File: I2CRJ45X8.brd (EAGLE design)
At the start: 80 x 50 mm, 54 parts, among them IC1 MCP23017SO, IC2 MCP23017SO, J1 M02X3-SHROUDED, J3 M02X3-PIN, J4 M02X3-PIN, J5 RJ45-X8, J6 M02X3-SHROUDED

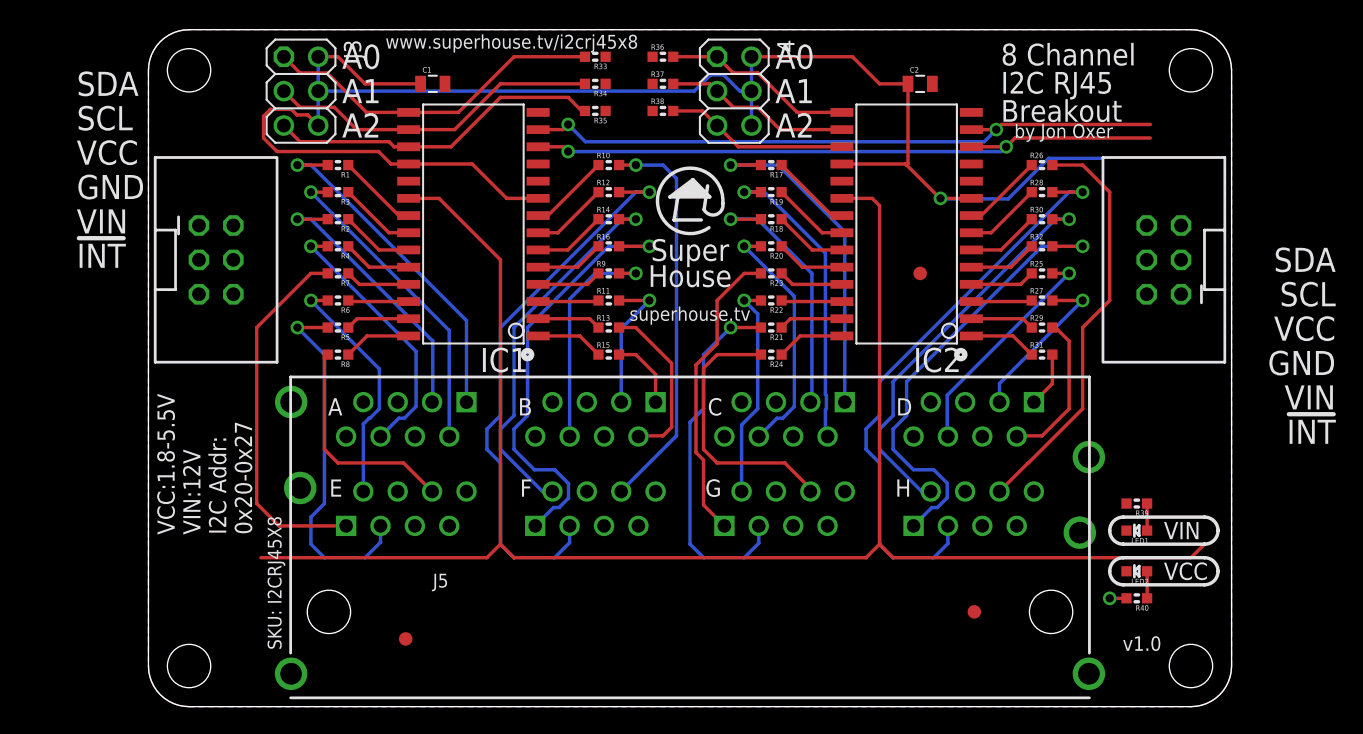
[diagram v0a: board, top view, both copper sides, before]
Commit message: Routing for I2C Breakout headers
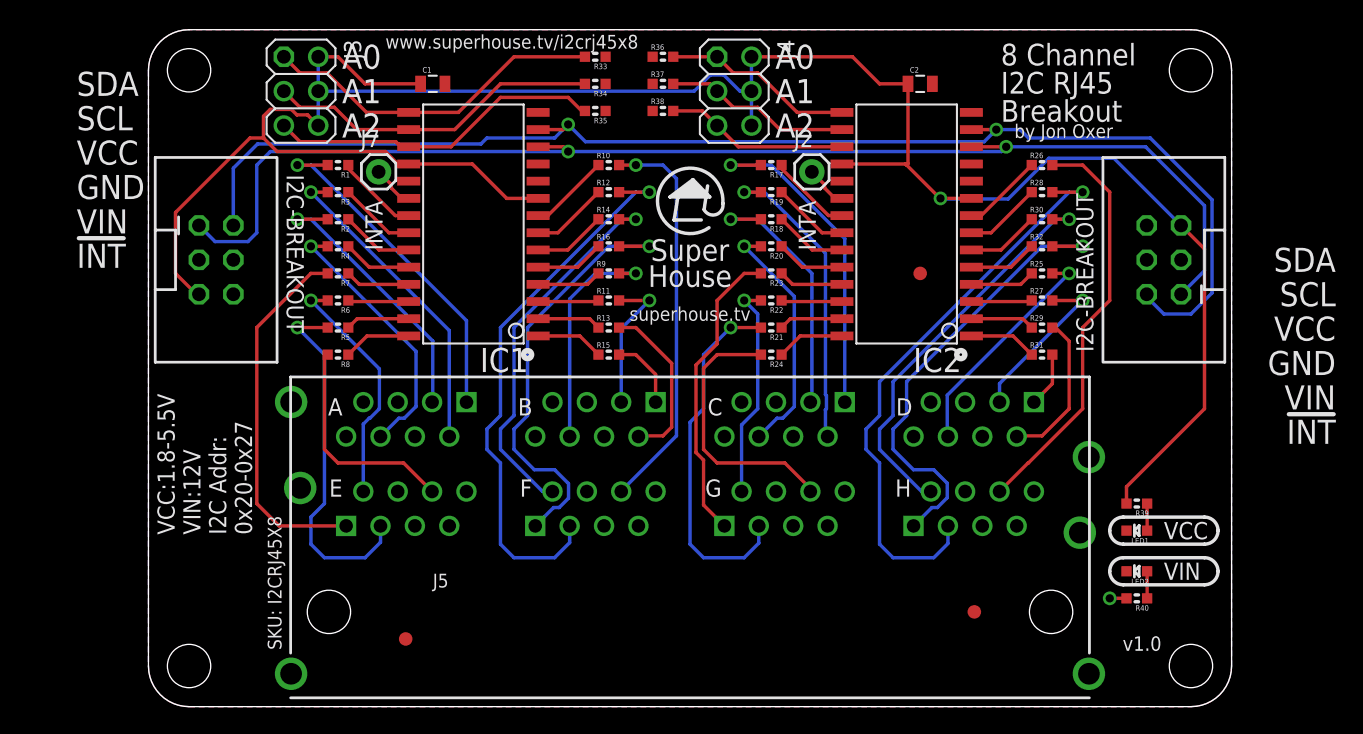
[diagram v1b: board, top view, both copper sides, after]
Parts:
- added J2: INT2A, SuperHouse-Connectors:1X01
- added J7: INT1A, SuperHouse-Connectors:1X01
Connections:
- removed net !INT: IC1.20, IC2.20
- new net N$10: IC1.20, J7.1
- new net N$9: IC2.20, J2.1
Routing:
- net !INT: track 129.4 -> 0.00 mm
- net SDA: track 48.3 -> 98.2 mm
- net VCC: track 122.6 -> 169.7 mm
- net SCL: track 48.3 -> 94.6 mm
- net N$9: track 0.00 -> 3.18 mm
- net N$10: track 0.00 -> 3.18 mm
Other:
- board text added: "I2C-BREAKOUT"
- board text added: "INTA"

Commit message: Experimenting with options for linking MCP reset to I2C Breakout reset
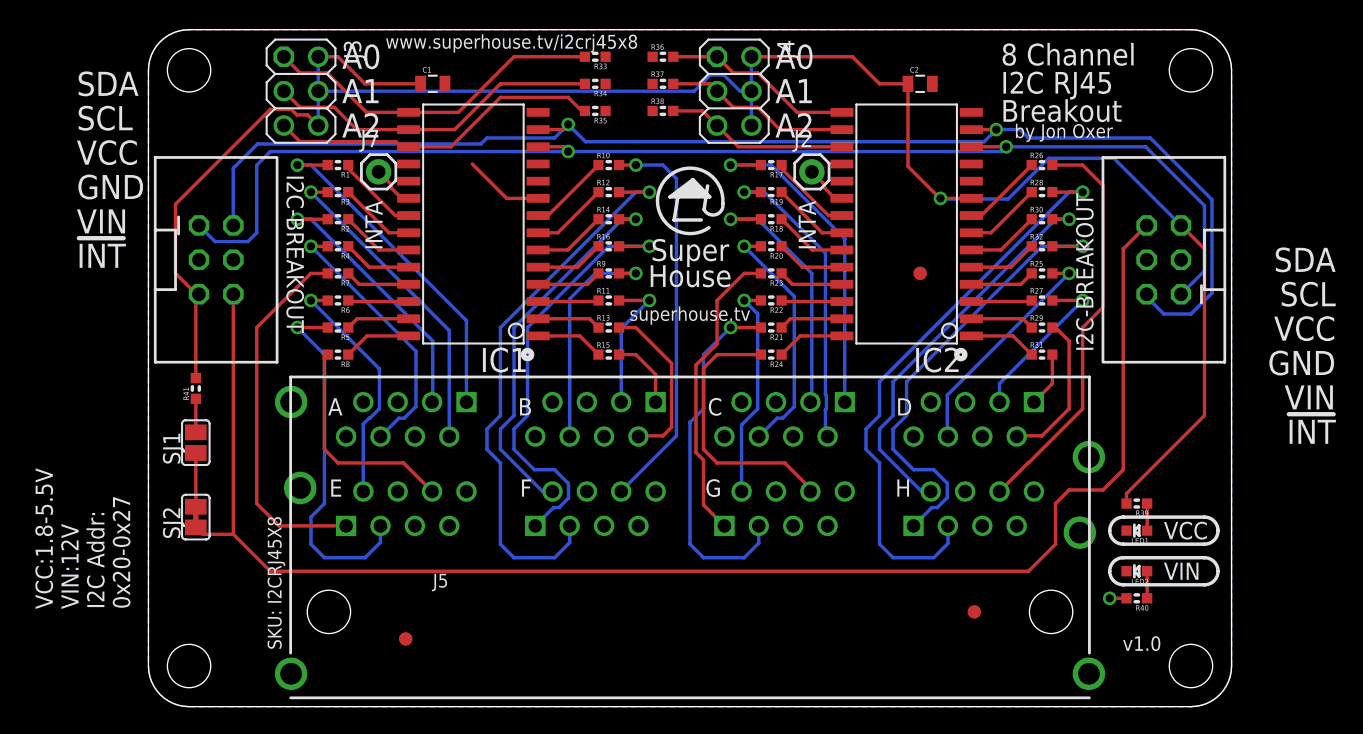
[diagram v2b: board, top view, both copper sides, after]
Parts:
- added R41: 10K, SuperHouse-DiscreteSemi:R0603
- added SJ1: (no value), SuperHouse-Jumpers:SJ
- added SJ2: SJC-NORMAL, SuperHouse-Jumpers:SJC
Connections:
- new net !RST: IC1.18, IC2.18, SJ1.1, SJ2.2
- new net N$14: R41.1, SJ1.2
- net !RESET: now also SJ2.1
- net VCC: now also R41.2; no longer IC1.18, IC2.18
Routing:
- net !RESET: track 0.00 -> 111.2 mm
- net VCC: track 169.7 -> 154.3 mm
- net !RST: track 0.00 -> 3.98 mm
- net N$14: track 0.00 -> 2.48 mm
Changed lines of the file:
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@@
 House</text>
 <text x="40" y="28.5" size="1.016" layer="21" font="vector" ratio="17" distance="20" align="bottom-center">superhouse.tv</text>
-<text x="4.16" y="12.7" size="1.27" layer="21" font="vector" ratio="18" rot="R90" align="center-left">VCC:1.8-5.5V
+<text x="-4.84" y="7.2" size="1.27" layer="21" font="vector" ratio="18" rot="R90" align="center-left">VCC:1.8-5.5V
 VIN:12V
 I2C Addr:
@@
 <attribute name="VALUE" x="15.73" y="36.325" size="1.27" layer="27"/>
 </element>
+<element name="SJ1" library="SuperHouse-Jumpers" library_urn="urn:adsk.eagle:library:12190622" package="SJ" package3d_urn="urn:adsk.eagle:package:7066338/1" value="" x="3.5" y="19.5" smashed="yes" rot="R90">
+<attribute name="NAME" x="2.357" y="17.849" size="1.27" layer="25" ratio="10" rot="R90"/>
+<attribute name="VALUE" x="3.5" y="19.9001" size="0.02" layer="27" rot="R90"/>
+</element>
+<element name="SJ2" library="SuperHouse-Jumpers" library_urn="urn:adsk.eagle:library:12190622" package="SJC" package3d_urn="urn:adsk.eagle:package:7066342/1" value="SJC-NORMAL" x="3.5" y="14" smashed="yes" rot="R90">
+<attribute name="NAME" x="2.357" y="12.349" size="1.27" layer="25" ratio="10" rot="R90"/>
+<attribute name="VALUE" x="3.5" y="14.4001" size="0.02" layer="27" rot="R90"/>
+</element>
+<element name="R41" library="SuperHouse-DiscreteSemi" library_urn="urn:adsk.eagle:library:11768461" package="R0603" package3d_urn="urn:adsk.eagle:package:11768543/2" value="10K" x="3.5" y="23.5" smashed="yes" rot="R90">
+<attribute name="NAME" x="2.992" y="22.611" size="0.4064" layer="25" font="vector" rot="R90"/>
+<attribute name="VALUE" x="4.4652" y="22.484" size="0.4064" layer="27" font="vector" rot="R90"/>
+</element>
 </elements>
 <signals>
@@
 <wire x1="65" y1="18" x2="69" y2="22" width="0.254" layer="1"/>
 <wire x1="69" y1="22" x2="69" y2="28" width="0.254" layer="1"/>
-<wire x1="69" y1="28" x2="71" y2="30" width="0.254" layer="1"/>
-<wire x1="71" y1="30" x2="71" y2="38" width="0.254" layer="1"/>
-<wire x1="71" y1="38" x2="69" y2="40" width="0.254" layer="1"/>
+<wire x1="69" y1="28" x2="70.5" y2="29.5" width="0.254" layer="1"/>
+<wire x1="70.5" y1="29.5" x2="70.5" y2="38.5" width="0.254" layer="1"/>
+<wire x1="70.5" y1="38.5" x2="69" y2="40" width="0.254" layer="1"/>
 <wire x1="69" y1="40" x2="66.762" y2="40" width="0.254" layer="1"/>
 </signal>
@@
 </signal>
 <signal name="VCC">
-<contactref element="IC1" pad="18"/>
 <contactref element="IC1" pad="9"/>
-<contactref element="IC2" pad="18"/>
 <contactref element="IC2" pad="9"/>
 <contactref element="J3" pad="6"/>
@@
 <contactref element="J3" pad="2"/>
 <wire x1="26.46" y1="37.54" x2="28.78" y2="37.54" width="0.254" layer="1"/>
-<wire x1="19.22" y1="40.08" x2="23.92" y2="40.08" width="0.254" layer="1"/>
 <wire x1="58.46" y1="37.54" x2="58.5" y2="37.54" width="0.254" layer="1"/>
 <wire x1="58.5" y1="37.54" x2="60.78" y2="37.54" width="0.254" layer="1"/>
-<wire x1="55.92" y1="40.08" x2="51.22" y2="40.08" width="0.254" layer="1"/>
 <contactref element="C1" pad="1"/>
-<wire x1="56" y1="40" x2="55.92" y2="40.08" width="0.254" layer="1"/>
 <wire x1="23.92" y1="40.08" x2="26.46" y2="37.54" width="0.254" layer="1"/>
-<wire x1="56" y1="40" x2="58.46" y2="37.54" width="0.254" layer="1"/>
 <contactref element="C2" pad="1"/>
-<wire x1="56.1" y1="46" x2="56.1" y2="40.1" width="0.254" layer="1"/>
-<wire x1="56.1" y1="40.1" x2="56" y2="40" width="0.254" layer="1"/>
 <contactref element="J4" pad="6"/>
 <contactref element="J4" pad="4"/>
@@
 <wire x1="54" y1="46" x2="52" y2="48" width="0.254" layer="1"/>
 <wire x1="52" y1="48" x2="44.54" y2="48" width="0.254" layer="1"/>
-<wire x1="19.22" y1="40.08" x2="18.42" y2="40.08" width="0.254" layer="1"/>
-<wire x1="18.42" y1="40.08" x2="17.5" y2="41" width="0.254" layer="1"/>
-<wire x1="9.5" y1="41" x2="8.5" y2="42" width="0.254" layer="1"/>
-<wire x1="8.5" y1="43.6138" x2="8.5" y2="42" width="0.254" layer="1"/>
-<wire x1="17.5" y1="41" x2="9.5" y2="41" width="0.254" layer="1"/>
 <wire x1="10.55593125" y1="44.1138" x2="9" y2="44.1138" width="0.254" layer="1"/>
-<wire x1="9" y1="44.1138" x2="8.5" y2="43.6138" width="0.254" layer="1"/>
 <wire x1="63.5" y1="37.5" x2="66.5" y2="40.5" width="0.254" layer="16"/>
 <wire x1="63.5" y1="37.5" x2="58.5" y2="37.5" width="0.254" layer="16"/>
@@
 <wire x1="71.31" y1="40.5" x2="76.27" y2="35.54" width="0.254" layer="16"/>
 <wire x1="66.5" y1="40.5" x2="71.31" y2="40.5" width="0.254" layer="16"/>
-<wire x1="72.238" y1="15" x2="72.238" y2="16.238" width="0.254" layer="1"/>
-<wire x1="72.238" y1="16.238" x2="78" y2="22" width="0.254" layer="1"/>
+<wire x1="72.238" y1="15" x2="72.238" y2="15.738" width="0.254" layer="1"/>
+<wire x1="72.238" y1="15.738" x2="78" y2="21.5" width="0.254" layer="1"/>
 <wire x1="78" y1="33.81" x2="76.27" y2="35.54" width="0.254" layer="1"/>
-<wire x1="78" y1="22" x2="78" y2="33.81" width="0.254" layer="1"/>
+<wire x1="78" y1="21.5" x2="78" y2="33.81" width="0.254" layer="1"/>
 <wire x1="3.73" y1="30.46" x2="3.54" y2="30.46" width="0.254" layer="1"/>
-<wire x1="3.54" y1="30.46" x2="2" y2="32" width="0.254" layer="1"/>
-<wire x1="2" y1="32" x2="2" y2="36.5" width="0.254" layer="1"/>
-<wire x1="2" y1="36.5" x2="7.5" y2="42" width="0.254" layer="1"/>
-<wire x1="7.5" y1="42" x2="8.5" y2="42" width="0.254" layer="1"/>
+<wire x1="2" y1="32" x2="3.54" y2="30.46" width="0.254" layer="1"/>
+<contactref element="R41" pad="2"/>
+<wire x1="9" y1="44.1138" x2="2" y2="37.1138" width="0.254" layer="1"/>
+<wire x1="2" y1="37.1138" x2="2" y2="32" width="0.254" layer="1"/>
+<wire x1="56.1" y1="39.9" x2="58.46" y2="37.54" width="0.254" layer="1"/>
+<wire x1="56.1" y1="46" x2="56.1" y2="39.9" width="0.254" layer="1"/>
+<wire x1="3.5" y1="24.262" x2="3.5" y2="30.23" width="0.254" layer="1"/>
+<wire x1="3.5" y1="30.23" x2="3.73" y2="30.46" width="0.254" layer="1"/>
+<wire x1="20.1" y1="46" x2="23.92" y2="40.08" width="0" layer="19" extent="1-1"/>
 </signal>
 <signal name="N$2">
@@
 <contactref element="J6" pad="6"/>
 <contactref element="J1" pad="6"/>
-<wire x1="6.27" y1="30.46" x2="73.73" y2="35.54" width="0" layer="19" extent="1-1"/>
+<contactref element="SJ2" pad="1"/>
+<wire x1="73.73" y1="35.54" x2="72" y2="33.81" width="0.254" layer="1"/>
+<wire x1="72" y1="17.5" x2="70.5" y2="16" width="0.254" layer="1"/>
+<wire x1="68" y1="16" x2="67" y2="15" width="0.254" layer="1"/>
+<wire x1="67" y1="12" x2="65" y2="10" width="0.254" layer="1"/>
+<wire x1="9" y1="10" x2="6.27" y2="12.73" width="0.254" layer="1"/>
+<wire x1="6.27" y1="12.73" x2="6.27" y2="30.46" width="0.254" layer="1"/>
+<wire x1="72" y1="33.81" x2="72" y2="17.5" width="0.254" layer="1"/>
+<wire x1="70.5" y1="16" x2="68" y2="16" width="0.254" layer="1"/>
+<wire x1="67" y1="15" x2="67" y2="12" width="0.254" layer="1"/>
+<wire x1="65" y1="10" x2="9" y2="10" width="0.254" layer="1"/>
+<wire x1="4.008" y1="12.73" x2="3.5" y2="13.238" width="0.254" layer="1"/>
+<wire x1="6.27" y1="12.73" x2="4.008" y2="12.73" width="0.254" layer="1"/>
 </signal>
 <signal name="N$9">
@@
 <wire x1="18.70434375" y1="37.54" x2="17.9382" y2="38.30614375" width="0.254" layer="1"/>
 </signal>
+<signal name="!RST">
+<contactref element="SJ1" pad="1"/>
+<contactref element="SJ2" pad="2"/>
+<contactref element="IC1" pad="18"/>
+<contactref element="IC2" pad="18"/>
+<wire x1="3.5" y1="18.738" x2="3.5" y2="14.762" width="0.254" layer="1"/>
+<wire x1="19.22" y1="40.08" x2="51.22" y2="40.08" width="0" layer="19" extent="1-1"/>
+<wire x1="3.5" y1="18.738" x2="19.22" y2="40.08" width="0" layer="19" extent="1-1"/>
+</signal>
+<signal name="N$14">
+<contactref element="R41" pad="1"/>
+<contactref element="SJ1" pad="2"/>
+<wire x1="3.5" y1="22.738" x2="3.5" y2="20.262" width="0.254" layer="1"/>
+</signal>
 </signals>
